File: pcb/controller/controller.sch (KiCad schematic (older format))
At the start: 44 parts

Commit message: Autofill passives
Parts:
- C? (x4): footprint (none) -> Capacitors_SMD:C_0402; Mouser (none) -> 710-885012105018
- C?: footprint (none) -> Capacitors_SMD:C_0402; Mouser (none) -> 81-GCQ1555C1H100RB1D
- C? (x3): footprint (none) -> Capacitors_SMD:C_0603_HandSoldering; Mouser (none) -> 810-CGB3B1X5R1A475MC
- C? (x2): footprint (none) -> Capacitors_SMD:C_0402; Mouser (none) -> 710-885012105003
- R? (x2): footprint (none) -> Resistors_SMD:R_0402; Mouser (none) -> 791-RMC1/16S-471JTH
- R?: footprint (none) -> Resistors_SMD:R_0603_HandSoldering; Mouser (none) -> 603-RC0603JR-0747KL
- R? (x2): footprint (none) -> Resistors_SMD:R_0402; Mouser (none) -> 603-RT0402FRE074K7L
- R? (x2): footprint (none) -> Resistors_SMD:R_0603_HandSoldering; Mouser (none) -> 755-ESR03EZPJ102
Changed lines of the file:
@@
 F 0 "C?" H 8109 4604 50  0000 R CNN
 F 1 "100nF" H 8109 4695 50  0000 R CNN
-F 2 "" H 8200 4650 50  0001 C CNN
+F 2 "Capacitors_SMD:C_0402" H 8200 4650 50  0001 C CNN
 F 3 "~" H 8200 4650 50  0001 C CNN
+F 4 "710-885012105018" H 8200 4650 50  0001 C CNN "Mouser"
 	1    8200 4650
 	1    0    0    1
@@
 F 0 "C?" H 7659 4604 50  0000 R CNN
 F 1 "100nF" H 7659 4695 50  0000 R CNN
-F 2 "" H 7750 4650 50  0001 C CNN
+F 2 "Capacitors_SMD:C_0402" H 7750 4650 50  0001 C CNN
 F 3 "~" H 7750 4650 50  0001 C CNN
+F 4 "710-885012105018" H 7750 4650 50  0001 C CNN "Mouser"
 	1    7750 4650
 	1    0    0    1
@@
 F 0 "C?" H 8809 1954 50  0000 R CNN
 F 1 "100nF" H 8809 2045 50  0000 R CNN
-F 2 "" H 8900 2000 50  0001 C CNN
+F 2 "Capacitors_SMD:C_0402" H 8900 2000 50  0001 C CNN
 F 3 "~" H 8900 2000 50  0001 C CNN
+F 4 "710-885012105018" H 8900 2000 50  0001 C CNN "Mouser"
 	1    8900 2000
 	-1   0    0    1
@@
 F 0 "C?" H 9259 1954 50  0000 R CNN
 F 1 "100nF" H 9259 2045 50  0000 R CNN
-F 2 "" H 9350 2000 50  0001 C CNN
+F 2 "Capacitors_SMD:C_0402" H 9350 2000 50  0001 C CNN
 F 3 "~" H 9350 2000 50  0001 C CNN
+F 4 "710-885012105018" H 9350 2000 50  0001 C CNN "Mouser"
 	1    9350 2000
 	-1   0    0    1
@@
 F 0 "C?" V 2571 4000 50  0000 C CNN
 F 1 "10pF" V 2662 4000 50  0000 C CNN
-F 2 "" H 2800 4000 50  0001 C CNN
+F 2 "Capacitors_SMD:C_0402" H 2800 4000 50  0001 C CNN
 F 3 "~" H 2800 4000 50  0001 C CNN
+F 4 "81-GCQ1555C1H100RB1D" H 2800 4000 50  0001 C CNN "Mouser"
 	1    2800 4000
 	0    1    1    0
@@
 F 0 "C?" H 1942 3696 50  0000 L CNN
 F 1 "4.7uF" H 1942 3605 50  0000 L CNN
-F 2 "" H 1850 3650 50  0001 C CNN
+F 2 "Capacitors_SMD:C_0603_HandSoldering" H 1850 3650 50  0001 C CNN
 F 3 "~" H 1850 3650 50  0001 C CNN
+F 4 "810-CGB3B1X5R1A475MC" H 1850 3650 50  0001 C CNN "Mouser"
 	1    1850 3650
 	1    0    0    -1
@@
 F 0 "R?" V 2896 5500 50  0000 C CNN
 F 1 "470" V 2805 5500 50  0000 C CNN
-F 2 "" H 2700 5500 50  0001 C CNN
+F 2 "Resistors_SMD:R_0402" H 2700 5500 50  0001 C CNN
 F 3 "~" H 2700 5500 50  0001 C CNN
+F 4 "791-RMC1/16S-471JTH" H 2700 5500 50  0001 C CNN "Mouser"
 	1    2700 5500
 	0    -1   -1   0
@@
 F 0 "R?" V 2896 5600 50  0000 C CNN
 F 1 "470" V 2805 5600 50  0000 C CNN
-F 2 "" H 2700 5600 50  0001 C CNN
+F 2 "Resistors_SMD:R_0402" H 2700 5600 50  0001 C CNN
 F 3 "~" H 2700 5600 50  0001 C CNN
+F 4 "791-RMC1/16S-471JTH" H 2700 5600 50  0001 C CNN "Mouser"
 	1    2700 5600
 	0    -1   1    0
@@
 F 0 "C?" H 2758 5904 50  0000 R CNN
 F 1 "0.33uF" H 2758 5995 50  0000 R CNN
-F 2 "" H 2850 5950 50  0001 C CNN
+F 2 "Capacitors_SMD:C_0402" H 2850 5950 50  0001 C CNN
 F 3 "~" H 2850 5950 50  0001 C CNN
+F 4 "710-885012105003" H 2850 5950 50  0001 C CNN "Mouser"
 	1    2850 5950
 	-1   0    0    1
@@
 F 0 "C?" H 2308 5904 50  0000 R CNN
 F 1 "0.33uF" H 2308 5995 50  0000 R CNN
-F 2 "" H 2400 5950 50  0001 C CNN
+F 2 "Capacitors_SMD:C_0402" H 2400 5950 50  0001 C CNN
 F 3 "~" H 2400 5950 50  0001 C CNN
+F 4 "710-885012105003" H 2400 5950 50  0001 C CNN "Mouser"
 	1    2400 5950
 	-1   0    0    1
@@
 F 0 "R?" H 5159 6946 50  0000 L CNN
 F 1 "47k" H 5159 6855 50  0000 L CNN
-F 2 "" H 5100 6900 50  0001 C CNN
+F 2 "Resistors_SMD:R_0603_HandSoldering" H 5100 6900 50  0001 C CNN
 F 3 "~" H 5100 6900 50  0001 C CNN
+F 4 "603-RC0603JR-0747KL" H 5100 6900 50  0001 C CNN "Mouser"
 	1    5100 6900
 	1    0    0    -1
@@
 F 0 "C?" V 6171 1300 50  0000 C CNN
 F 1 "4.7uF" V 6262 1300 50  0000 C CNN
-F 2 "" H 6400 1300 50  0001 C CNN
+F 2 "Capacitors_SMD:C_0603_HandSoldering" H 6400 1300 50  0001 C CNN
 F 3 "~" H 6400 1300 50  0001 C CNN
+F 4 "810-CGB3B1X5R1A475MC" H 6400 1300 50  0001 C CNN "Mouser"
 	1    6400 1300
 	0    1    1    0
@@
 F 0 "R?" V 2846 4750 50  0000 C CNN
 F 1 "4.7k" V 2755 4750 50  0000 C CNN
-F 2 "" H 2650 4750 50  0001 C CNN
+F 2 "Resistors_SMD:R_0402" H 2650 4750 50  0001 C CNN
 F 3 "~" H 2650 4750 50  0001 C CNN
+F 4 "603-RT0402FRE074K7L" H 2650 4750 50  0001 C CNN "Mouser"
 	1    2650 4750
 	0    1    1    0
@@
 F 0 "C?" H 9842 2046 50  0000 L CNN
 F 1 "4.7uF" H 9842 1955 50  0000 L CNN
-F 2 "" H 9750 2000 50  0001 C CNN
+F 2 "Capacitors_SMD:C_0603_HandSoldering" H 9750 2000 50  0001 C CNN
 F 3 "~" H 9750 2000 50  0001 C CNN
+F 4 "810-CGB3B1X5R1A475MC" H 9750 2000 50  0001 C CNN "Mouser"
 	1    9750 2000
 	1    0    0    -1
@@
 F 0 "R?" V 3646 5000 50  0000 C CNN
 F 1 "1k" V 3555 5000 50  0000 C CNN
-F 2 "" H 3450 5000 50  0001 C CNN
+F 2 "Resistors_SMD:R_0603_HandSoldering" H 3450 5000 50  0001 C CNN
 F 3 "~" H 3450 5000 50  0001 C CNN
+F 4 "755-ESR03EZPJ102" H 3450 5000 50  0001 C CNN "Mouser"
 	1    3450 5000
 	0    -1   -1   0
@@
 F 0 "R?" V 6796 2600 50  0000 C CNN
 F 1 "4.7k" V 6705 2600 50  0000 C CNN
-F 2 "" H 6600 2600 50  0001 C CNN
+F 2 "Resistors_SMD:R_0402" H 6600 2600 50  0001 C CNN
 F 3 "~" H 6600 2600 50  0001 C CNN
+F 4 "603-RT0402FRE074K7L" H 6600 2600 50  0001 C CNN "Mouser"
 	1    6600 2600
 	-1   0    0    1
@@
 F 0 "R?" H 6209 1846 50  0000 L CNN
 F 1 "1k" H 6209 1755 50  0000 L CNN
-F 2 "" H 6150 1800 50  0001 C CNN
+F 2 "Resistors_SMD:R_0603_HandSoldering" H 6150 1800 50  0001 C CNN
 F 3 "~" H 6150 1800 50  0001 C CNN
+F 4 "755-ESR03EZPJ102" H 6150 1800 50  0001 C CNN "Mouser"
 	1    6150 1800
 	1    0    0    -1

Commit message: Add footprints
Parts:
- removed J?: Conn_01x02, symbol Connector_Generic:Conn_01x02
- added D?: LED, Socket_Strips:Socket_Strip_Straight_1x02_Pitch1.27mm, symbol Device:LED
- J3: renamed from J?; footprint (none) -> Socket_Strips:Socket_Strip_Straight_1x03_Pitch1.27mm; Mouser (none) -> NoPart
- Q3: renamed from Q?; value Q_NPN_BEC -> BC847BLT1G
- U2: renamed from U?; Mouser (none) -> 511-LIS2DE12TR
- U3: renamed from U?; Mouser (none) -> 595-430FR2512IRHLR
- gave numbers to parts that had none: 39
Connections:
- wire segments 154 -> 151
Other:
- moved on the sheet: C1

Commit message: All parts (I think?) sourced and footprinted
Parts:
- removed Q1, Q2: Q_PMOS_DGS, symbol Device:Q_PMOS_DGS
- added Q?: CSD25481F4T, controller:TI_Femto0402, symbol Device:Q_PMOS_GSD
- added Q?: RU1C001ZPTL, controller:Rohm_UMT3F, symbol Device:Q_PMOS_GSD
- J4: footprint (none) -> Socket_Strips:Socket_Strip_Straight_2x02_Pitch1.27mm
- L1: footprint (none) -> Inductors:Inductor_Taiyo-Yuden_NR-24xx_HandSoldering; Mouser (none) -> 963-NRH2410T4R7MN
- MH1: footprint (none) -> Mounting_Holes:MountingHole_3.2mm_M3; Mouser (none) -> NoPart
- U1: footprint (none) -> TO_SOT_Packages_SMD:SOT-23-5_HandSoldering; Mouser (none) -> 595-TPS613222ADBVR
- U2: footprint (none) -> controller:ST_LGA12
- U3: footprint (none) -> controller:TI_MSP430_VQFN20
- U4: footprint (none) -> controller:Bosch_LGA14; Mouser (none) -> 262-BMG250
- Y1: footprint (none) -> Crystals:Crystal_DS26_d2.0mm_l6.0mm_Horizontal; Mouser (none) -> 520-ECS327-6-13-X
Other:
- note removed: "TODO source"
- note removed: "TODO: make sure the pins are right!!"
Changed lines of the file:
@@
 F 0 "U2" H 7900 3315 50  0000 C CNN
 F 1 "LIS2DE12TR" H 7900 3224 50  0000 C CNN
-F 2 "" H 7900 2850 50  0001 C CNN
+F 2 "controller:ST_LGA12" H 7900 2850 50  0001 C CNN
 F 3 "" H 7900 2850 50  0001 C CNN
 F 4 "511-LIS2DE12TR" H 7900 2850 50  0001 C CNN "Mouser"
@@
 F 0 "U4" H 8850 5615 50  0000 C CNN
 F 1 "BMG250" H 8850 5524 50  0000 C CNN
-F 2 "" H 8850 5150 50  0001 C CNN
+F 2 "controller:Bosch_LGA14" H 8850 5150 50  0001 C CNN
 F 3 "" H 8850 5150 50  0001 C CNN
+F 4 "262-BMG250" H 8850 5150 50  0001 C CNN "Mouser"
 	1    8850 5150
 	1    0    0    -1
@@
 F 0 "U1" H 3925 1915 50  0000 C CNN
 F 1 "TPS613222ADBVR" H 3925 1824 50  0000 C CNN
-F 2 "" H 3900 1650 50  0001 C CNN
+F 2 "TO_SOT_Packages_SMD:SOT-23-5_HandSoldering" H 3900 1650 50  0001 C CNN
 F 3 "" H 3900 1650 50  0001 C CNN
+F 4 "595-TPS613222ADBVR" H 3900 1650 50  0001 C CNN "Mouser"
 	1    3900 1650
 	1    0    0    -1
@@
 F 0 "L1" V 3535 1650 50  0000 C CNN
 F 1 "4.7uH" V 3444 1650 50  0000 C CNN
-F 2 "" H 3350 1650 50  0001 C CNN
+F 2 "Inductors:Inductor_Taiyo-Yuden_NR-24xx_HandSoldering" H 3350 1650 50  0001 C CNN
 F 3 "~" H 3350 1650 50  0001 C CNN
+F 4 "963-NRH2410T4R7MN" V 3350 1650 50  0001 C CNN "Mouser"
 	1    3350 1650
 	0    -1   -1   0
@@
 	4800 1650 4500 1650
 Connection ~ 4500 1650
-$Comp
-L Device:Q_PMOS_DGS Q2
-U 1 1 5B81CA73
-P 2600 1750
-F 0 "Q2" V 2943 1750 50  0000 C CNN
-F 1 "Q_PMOS_DGS" V 2852 1750 50  0000 C CNN
-F 2 "" H 2800 1850 50  0001 C CNN
-F 3 "~" H 2600 1750 50  0001 C CNN
-	1    2600 1750
-	0    1    -1   0
-$EndComp
-Text Notes 1750 1350 0    50   ~ 0
-TODO: make sure the pins are right!!
 Wire Wire Line
 	2800 1650 3150 1650
@@
 F 0 "U3" H 5075 4865 50  0000 C CNN
 F 1 "MSP430FR2512IRHLR" H 5075 4774 50  0000 C CNN
-F 2 "" H 4900 4800 50  0001 C CNN
+F 2 "controller:TI_MSP430_VQFN20" H 4900 4800 50  0001 C CNN
 F 3 "" H 4900 4800 50  0001 C CNN
 	2    4900 4800
@@
 F 0 "Y1" V 3004 4069 50  0000 R CNN
 F 1 "32.786kHz" V 3095 4069 50  0000 R CNN
-F 2 "" H 3050 4200 50  0001 C CNN
+F 2 "Crystals:Crystal_DS26_d2.0mm_l6.0mm_Horizontal" H 3050 4200 50  0001 C CNN
 F 3 "~" H 3050 4200 50  0001 C CNN
+F 4 "520-ECS327-6-13-X" V 3050 4200 50  0001 C CNN "Mouser"
 	1    3050 4200
 	0    -1   1    0
@@
 F 0 "U3" H 5719 2746 50  0000 L CNN
 F 1 "MSP430FR2512IRHLR" H 5719 2655 50  0000 L CNN
-F 2 "" H 4900 3350 50  0001 C CNN
+F 2 "controller:TI_MSP430_VQFN20" H 4900 3350 50  0001 C CNN
 F 3 "" H 4900 3350 50  0001 C CNN
 F 4 "595-430FR2512IRHLR" H 4900 3350 50  0001 C CNN "Mouser"
@@
 F 0 "J4" H 3650 7167 50  0000 C CNN
 F 1 "Conn_02x02_Odd_Even" H 3650 7076 50  0000 C CNN
-F 2 "" H 3600 6950 50  0001 C CNN
+F 2 "Socket_Strips:Socket_Strip_Straight_2x02_Pitch1.27mm" H 3600 6950 50  0001 C CNN
 F 3 "~" H 3600 6950 50  0001 C CNN
 	1    3600 6950
@@
 F 0 "MH1" H 1300 6946 50  0000 L CNN
 F 1 "MountingHole" H 1300 6855 50  0000 L CNN
-F 2 "" H 1200 6900 50  0001 C CNN
+F 2 "Mounting_Holes:MountingHole_3.2mm_M3" H 1200 6900 50  0001 C CNN
 F 3 "~" H 1200 6900 50  0001 C CNN
+F 4 "NoPart" H 1200 6900 50  0001 C CNN "Mouser"
 	1    1200 6900
 	1    0    0    -1
@@
 Text Label 3050 6950 0    50   ~ 0
 +VBAT
-Text Notes 3250 1400 0    50   ~ 0
-TODO source
 Text Label 5200 7100 0    50   ~ 0
 SBWTDIO
@@
 	0    1    -1   0
 $EndComp
-$Comp
-L Device:Q_PMOS_DGS Q1
-U 1 1 5BA6F00A
-P 1500 1750
-F 0 "Q1" V 1843 1750 50  0000 C CNN
-F 1 "Q_PMOS_DGS" V 1752 1750 50  0000 C CNN
-F 2 "" H 1700 1850 50  0001 C CNN
-F 3 "~" H 1500 1750 50  0001 C CNN
-	1    1500 1750
-	0    -1   -1   0
-$EndComp
 Wire Wire Line
 	1700 1650 2000 1650
 Connection ~ 2000 1650
-Text Notes 1300 1450 0    50   ~ 0
-TODO: make sure the pins are right!!
 $Comp
 L power:GND #PWR0128
@@
 	0    -1   -1   0
 $EndComp
+$Comp
+L Device:Q_PMOS_GSD Q?
+U 1 1 5B8C3C91
+P 2600 1750
+F 0 "Q?" V 2943 1750 50  0000 C CNN
+F 1 "CSD25481F4T" V 2852 1750 50  0000 C CNN
+F 2 "controller:TI_Femto0402" H 2800 1850 50  0001 C CNN
+F 3 "~" H 2600 1750 50  0001 C CNN
+F 4 "595-CSD25481F4T" V 2600 1750 50  0001 C CNN "Mouser"
+	1    2600 1750
+	0    1    -1   0
+$EndComp
+$Comp
+L Device:Q_PMOS_GSD Q?
+U 1 1 5B8CAC5E
+P 1500 1750
+F 0 "Q?" V 1843 1750 50  0000 C CNN
+F 1 "RU1C001ZPTL" V 1752 1750 50  0000 C CNN
+F 2 "controller:Rohm_UMT3F" H 1700 1850 50  0001 C CNN
+F 3 "~" H 1500 1750 50  0001 C CNN
+F 4 "755-RU1C001ZPTL" V 1500 1750 50  0001 C CNN "Mouser"
+	1    1500 1750
+	0    -1   -1   0
+$EndComp

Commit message: Now all parts footprinted and sourced
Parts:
- J2: footprint (none) -> Socket_Strips:Socket_Strip_Straight_1x02_Pitch1.27mm; Mouser (none) -> NoPart
- J4: Mouser (none) -> NoPart
- MH2: footprint (none) -> Mounting_Holes:MountingHole_3.2mm_M3; Mouser (none) -> NoPart
- U3: Mouser (none) -> 595-430FR2512IRHLR
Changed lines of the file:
@@
 F 0 "J2" H 770 1867 50  0000 C CNN
 F 1 "Conn_01x02" H 770 1776 50  0000 C CNN
-F 2 "" H 850 1650 50  0001 C CNN
+F 2 "Socket_Strips:Socket_Strip_Straight_1x02_Pitch1.27mm" H 850 1650 50  0001 C CNN
 F 3 "~" H 850 1650 50  0001 C CNN
+F 4 "NoPart" H 850 1650 50  0001 C CNN "Mouser"
 	1    850  1650
 	-1   0    0    -1
@@
 F 2 "controller:TI_MSP430_VQFN20" H 4900 4800 50  0001 C CNN
 F 3 "" H 4900 4800 50  0001 C CNN
+F 4 "595-430FR2512IRHLR" H 4900 4800 50  0001 C CNN "Mouser"
 	2    4900 4800
 	1    0    0    -1
@@
 F 2 "Socket_Strips:Socket_Strip_Straight_2x02_Pitch1.27mm" H 3600 6950 50  0001 C CNN
 F 3 "~" H 3600 6950 50  0001 C CNN
+F 4 "NoPart" H 3600 6950 50  0001 C CNN "Mouser"
 	1    3600 6950
 	1    0    0    -1
@@
 F 0 "MH2" H 1300 7246 50  0000 L CNN
 F 1 "MountingHole" H 1300 7155 50  0000 L CNN
-F 2 "" H 1200 7200 50  0001 C CNN
+F 2 "Mounting_Holes:MountingHole_3.2mm_M3" H 1200 7200 50  0001 C CNN
 F 3 "~" H 1200 7200 50  0001 C CNN
+F 4 "NoPart" H 1200 7200 50  0001 C CNN "Mouser"
 	1    1200 7200
 	1    0    0    -1

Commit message: Finish layout and generate Gerbers
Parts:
- removed MH1, MH2: MountingHole, Mounting_Holes:MountingHole_3.2mm_M3, symbol Mechanical:MountingHole
- added J1: Conn_01x01, Socket_Strips:Socket_Strip_Straight_1x01_Pitch2.54mm, symbol Connector_Generic:Conn_01x01
- added R12: 4.7k, Resistors_SMD:R_0402, symbol Device:R_Small
- gave numbers to parts that had none: 3
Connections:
- wire segments 151 -> 160
- no-connect marks 8 -> 13
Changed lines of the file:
@@
 L power:GND #PWR0101
 U 1 1 5B819CCE
-P 8100 3450
-F 0 "#PWR0101" H 8100 3200 50  0001 C CNN
-F 1 "GND" H 8105 3277 50  0000 C CNN
-F 2 "" H 8100 3450 50  0001 C CNN
-F 3 "" H 8100 3450 50  0001 C CNN
-	1    8100 3450
-	1    0    0    -1
-$EndComp
-Wire Wire Line
-	8100 3350 8100 3400
+P 8000 3450
+F 0 "#PWR0101" H 8000 3200 50  0001 C CNN
+F 1 "GND" H 8005 3277 50  0000 C CNN
+F 2 "" H 8000 3450 50  0001 C CNN
+F 3 "" H 8000 3450 50  0001 C CNN
+	1    8000 3450
+	1    0    0    -1
+$EndComp
 Wire Wire Line
 	8000 3350 8000 3400
 Wire Wire Line
-	8000 3400 8100 3400
-Connection ~ 8100 3400
-Wire Wire Line
-	8100 3400 8100 3450
-Wire Wire Line
 	7900 3350 7900 3400
 Wire Wire Line
 	7900 3400 8000 3400
-Connection ~ 8000 3400
 Wire Wire Line
 	7800 3350 7800 3400
@@
 	3450 1650 3550 1650
 Wire Wire Line
-	3250 1650 3150 1650
+	3250 1650 3200 1650
 Wire Wire Line
 	3150 1650 3150 1750
@@
 $EndComp
 Wire Wire Line
-	1150 1850 1150 1750
+	1150 1850 1150 1800
 Wire Wire Line
 	1150 1750 1050 1750
@@
 	2800 1650 3150 1650
 Wire Wire Line
-	1050 1650 1300 1650
+	1050 1650 1200 1650
 $Comp
 L Device:R_Small R3
@@
 $EndComp
 $Comp
-L Mechanical:MountingHole MH1
-U 1 1 5B91C86E
-P 1200 6900
-F 0 "MH1" H 1300 6946 50  0000 L CNN
-F 1 "MountingHole" H 1300 6855 50  0000 L CNN
-F 2 "Mounting_Holes:MountingHole_3.2mm_M3" H 1200 6900 50  0001 C CNN
-F 3 "~" H 1200 6900 50  0001 C CNN
-F 4 "NoPart" H 1200 6900 50  0001 C CNN "Mouser"
-	1    1200 6900
-	1    0    0    -1
-$EndComp
-$Comp
-L Mechanical:MountingHole MH2
-U 1 1 5B91C8C6
-P 1200 7200
-F 0 "MH2" H 1300 7246 50  0000 L CNN
-F 1 "MountingHole" H 1300 7155 50  0000 L CNN
-F 2 "Mounting_Holes:MountingHole_3.2mm_M3" H 1200 7200 50  0001 C CNN
-F 3 "~" H 1200 7200 50  0001 C CNN
-F 4 "NoPart" H 1200 7200 50  0001 C CNN "Mouser"
-	1    1200 7200
-	1    0    0    -1
-$EndComp
-$Comp
 L power:GND #PWR0122
 U 1 1 5B91CC97
@@
 	2000 1750 2000 1650
 Wire Wire Line
-	2000 1650 2300 1650
+	2000 1650 2200 1650
 $Comp
 L Device:C_Small C1
@@
 L power:GND #PWR0127
 U 1 1 5B9D40C5
-P 8150 5250
-F 0 "#PWR0127" H 8150 5000 50  0001 C CNN
-F 1 "GND" V 8155 5122 50  0000 R CNN
-F 2 "" H 8150 5250 50  0001 C CNN
-F 3 "" H 8150 5250 50  0001 C CNN
-	1    8150 5250
+P 7800 5250
+F 0 "#PWR0127" H 7800 5000 50  0001 C CNN
+F 1 "GND" V 7805 5122 50  0000 R CNN
+F 2 "" H 7800 5250 50  0001 C CNN
+F 3 "" H 7800 5250 50  0001 C CNN
+	1    7800 5250
 	0    1    1    0
 $EndComp
@@
 	1500 1950 1500 2050
 $Comp
-L Device:LED D?
+L Device:LED D1
 U 1 1 5B8A851C
 P 6150 1450
-F 0 "D?" V 6188 1333 50  0000 R CNN
+F 0 "D1" V 6188 1333 50  0000 R CNN
 F 1 "LED" V 6097 1333 50  0000 R CNN
 F 2 "Socket_Strips:Socket_Strip_Straight_1x02_Pitch1.27mm" H 6150 1450 50  0001 C CNN
@@
 $EndComp
 $Comp
-L Device:Q_PMOS_GSD Q?
+L Device:Q_PMOS_GSD Q2
 U 1 1 5B8C3C91
 P 2600 1750
-F 0 "Q?" V 2943 1750 50  0000 C CNN
+F 0 "Q2" V 2943 1750 50  0000 C CNN
 F 1 "CSD25481F4T" V 2852 1750 50  0000 C CNN
 F 2 "controller:TI_Femto0402" H 2800 1850 50  0001 C CNN
@@
 $EndComp
 $Comp
-L Device:Q_PMOS_GSD Q?
+L Device:Q_PMOS_GSD Q1
 U 1 1 5B8CAC5E
 P 1500 1750
-F 0 "Q?" V 1843 1750 50  0000 C CNN
+F 0 "Q1" V 1843 1750 50  0000 C CNN
 F 1 "RU1C001ZPTL" V 1752 1750 50  0000 C CNN
 F 2 "controller:Rohm_UMT3F" H 1700 1850 50  0001 C CNN
@@
 	0    -1   -1   0
 $EndComp
+NoConn ~ 3800 3650
+NoConn ~ 3800 5300
+NoConn ~ 3800 5400
+NoConn ~ 3800 5800
+NoConn ~ 3800 5900
+$Comp
+L Connector_Generic:Conn_01x01 J1
+U 1 1 5B902E19
+P 2450 3100
+F 0 "J1" H 2370 2875 50  0000 C CNN
+F 1 "Conn_01x01" H 2370 2966 50  0000 C CNN
+F 2 "Socket_Strips:Socket_Strip_Straight_1x01_Pitch2.54mm" H 2450 3100 50  0001 C CNN
+F 3 "~" H 2450 3100 50  0001 C CNN
+F 4 "NoPart" H 2450 3100 50  0001 C CNN "Mouser"
+	1    2450 3100
+	-1   0    0    1
+$EndComp
+Text Label 3100 3100 2    50   ~ 0
+CAP
+Wire Wire Line
+	3100 3100 2650 3100
+$Comp
+L power:PWR_FLAG #FLG0101
+U 1 1 5B90A3E0
+P 1200 1450
+F 0 "#FLG0101" H 1200 1525 50  0001 C CNN
+F 1 "PWR_FLAG" H 1200 1624 50  0000 C CNN
+F 2 "" H 1200 1450 50  0001 C CNN
+F 3 "~" H 1200 1450 50  0001 C CNN
+	1    1200 1450
+	1    0    0    -1
+$EndComp
+$Comp
+L power:PWR_FLAG #FLG0102
+U 1 1 5B90A44C
+P 2200 1450
+F 0 "#FLG0102" H 2200 1525 50  0001 C CNN
+F 1 "PWR_FLAG" H 2200 1624 50  0000 C CNN
+F 2 "" H 2200 1450 50  0001 C CNN
+F 3 "~" H 2200 1450 50  0001 C CNN
+	1    2200 1450
+	1    0    0    -1
+$EndComp
+$Comp
+L power:PWR_FLAG #FLG0103
+U 1 1 5B90A4B1
+P 3200 1450
+F 0 "#FLG0103" H 3200 1525 50  0001 C CNN
+F 1 "PWR_FLAG" H 3200 1624 50  0000 C CNN
+F 2 "" H 3200 1450 50  0001 C CNN
+F 3 "~" H 3200 1450 50  0001 C CNN
+	1    3200 1450
+	1    0    0    -1
+$EndComp
+$Comp
+L power:PWR_FLAG #FLG0104
+U 1 1 5B90A516
+P 1000 2050
+F 0 "#FLG0104" H 1000 2125 50  0001 C CNN
+F 1 "PWR_FLAG" H 1000 2223 50  0000 C CNN
+F 2 "" H 1000 2050 50  0001 C CNN
+F 3 "~" H 1000 2050 50  0001 C CNN
+	1    1000 2050
+	-1   0    0    1
+$EndComp
+Wire Wire Line
+	1000 2050 1000 1800
+Wire Wire Line
+	1000 1800 1150 1800
+Connection ~ 1150 1800
+Wire Wire Line
+	1150 1800 1150 1750
+Wire Wire Line
+	1200 1450 1200 1650
+Connection ~ 1200 1650
+Wire Wire Line
+	1200 1650 1300 1650
+Wire Wire Line
+	2200 1450 2200 1650
+Connection ~ 2200 1650
+Wire Wire Line
+	2200 1650 2300 1650
+Wire Wire Line
+	3200 1450 3200 1650
+Connection ~ 3200 1650
+Wire Wire Line
+	3200 1650 3150 1650
+$Comp
+L Device:R_Small R12
+U 1 1 5B927701
+P 8050 5250
+F 0 "R12" V 8246 5250 50  0000 C CNN
+F 1 "4.7k" V 8155 5250 50  0000 C CNN
+F 2 "Resistors_SMD:R_0402" H 8050 5250 50  0001 C CNN
+F 3 "~" H 8050 5250 50  0001 C CNN
+F 4 "603-RT0402FRE074K7L" V 8050 5250 50  0001 C CNN "Mouser"
+	1    8050 5250
+	0    -1   -1   0
+$EndComp
+Wire Wire Line
+	7950 5250 7800 5250
+Wire Wire Line
+	8000 3450 8000 3400
+Connection ~ 8000 3400
 $EndSCHEMATC

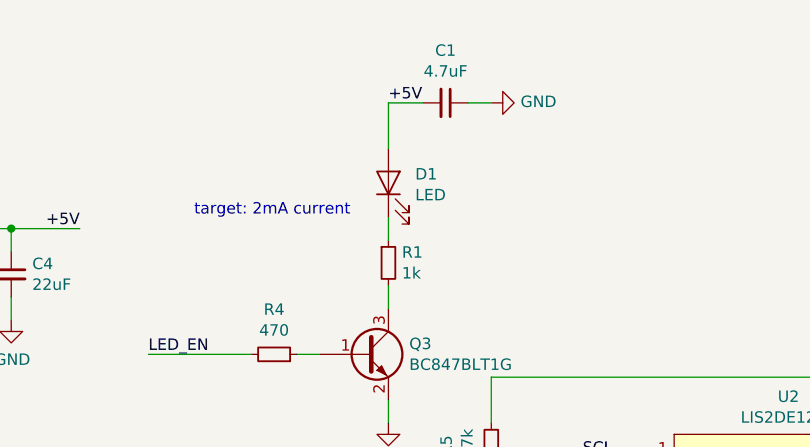
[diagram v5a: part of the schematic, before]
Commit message: Add simulation results
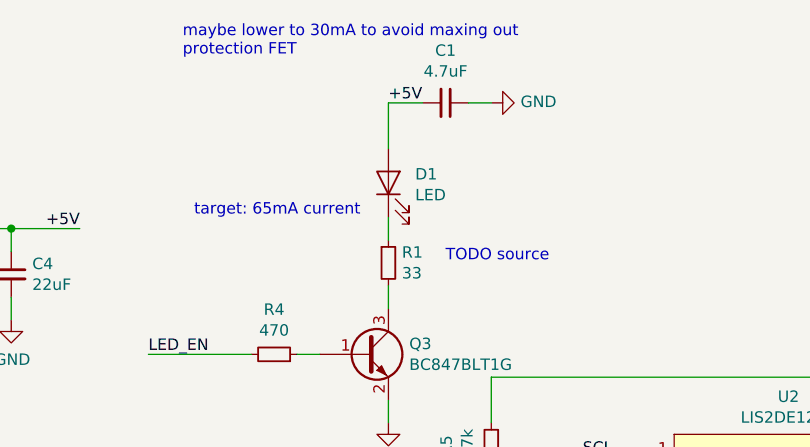
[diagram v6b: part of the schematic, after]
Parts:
- D1: Mouser NoPart -> 941-JB3030W00A0UC435
- R1: value 1k -> 33; Mouser 755-ESR03EZPJ102 -> (none)
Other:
- note added: "TODO source"
- note added: "maybe lower to 30mA to avoid maxing out \nprotection FET"
- note added: "target: 65mA current"
- note removed: "target: 2mA current"
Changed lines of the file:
@@
 $EndComp
 Text Notes 5300 1600 0    50   ~ 0
-target: 2mA current
+target: 65mA current
 Text Notes 1650 5600 0    50   ~ 0
 UART
@@
 P 6150 1800
 F 0 "R1" H 6209 1846 50  0000 L CNN
-F 1 "1k" H 6209 1755 50  0000 L CNN
+F 1 "33" H 6209 1755 50  0000 L CNN
 F 2 "Resistors_SMD:R_0603_HandSoldering" H 6150 1800 50  0001 C CNN
 F 3 "~" H 6150 1800 50  0001 C CNN
-F 4 "755-ESR03EZPJ102" H 6150 1800 50  0001 C CNN "Mouser"
 	1    6150 1800
 	1    0    0    -1
@@
 F 2 "Socket_Strips:Socket_Strip_Straight_1x02_Pitch1.27mm" H 6150 1450 50  0001 C CNN
 F 3 "~" H 6150 1450 50  0001 C CNN
-F 4 "NoPart" V 6150 1450 50  0001 C CNN "Mouser"
+F 4 "941-JB3030W00A0UC435" V 6150 1450 50  0001 C CNN "Mouser"
 	1    6150 1450
 	0    -1   -1   0
@@
 	8000 3450 8000 3400
 Connection ~ 8000 3400
+Text Notes 6400 1800 0    50   ~ 0
+TODO source
+Text Notes 5250 900  0    50   ~ 0
+maybe lower to 30mA to avoid maxing out \nprotection FET
 $EndSCHEMATC
